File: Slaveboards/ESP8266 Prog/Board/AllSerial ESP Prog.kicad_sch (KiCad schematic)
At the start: 13 parts, among them T1 BC847, T2 BC847, X1 ALLSERIALSLAVE, X2 PinSocket_2x04_P2.54mm_Horizo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

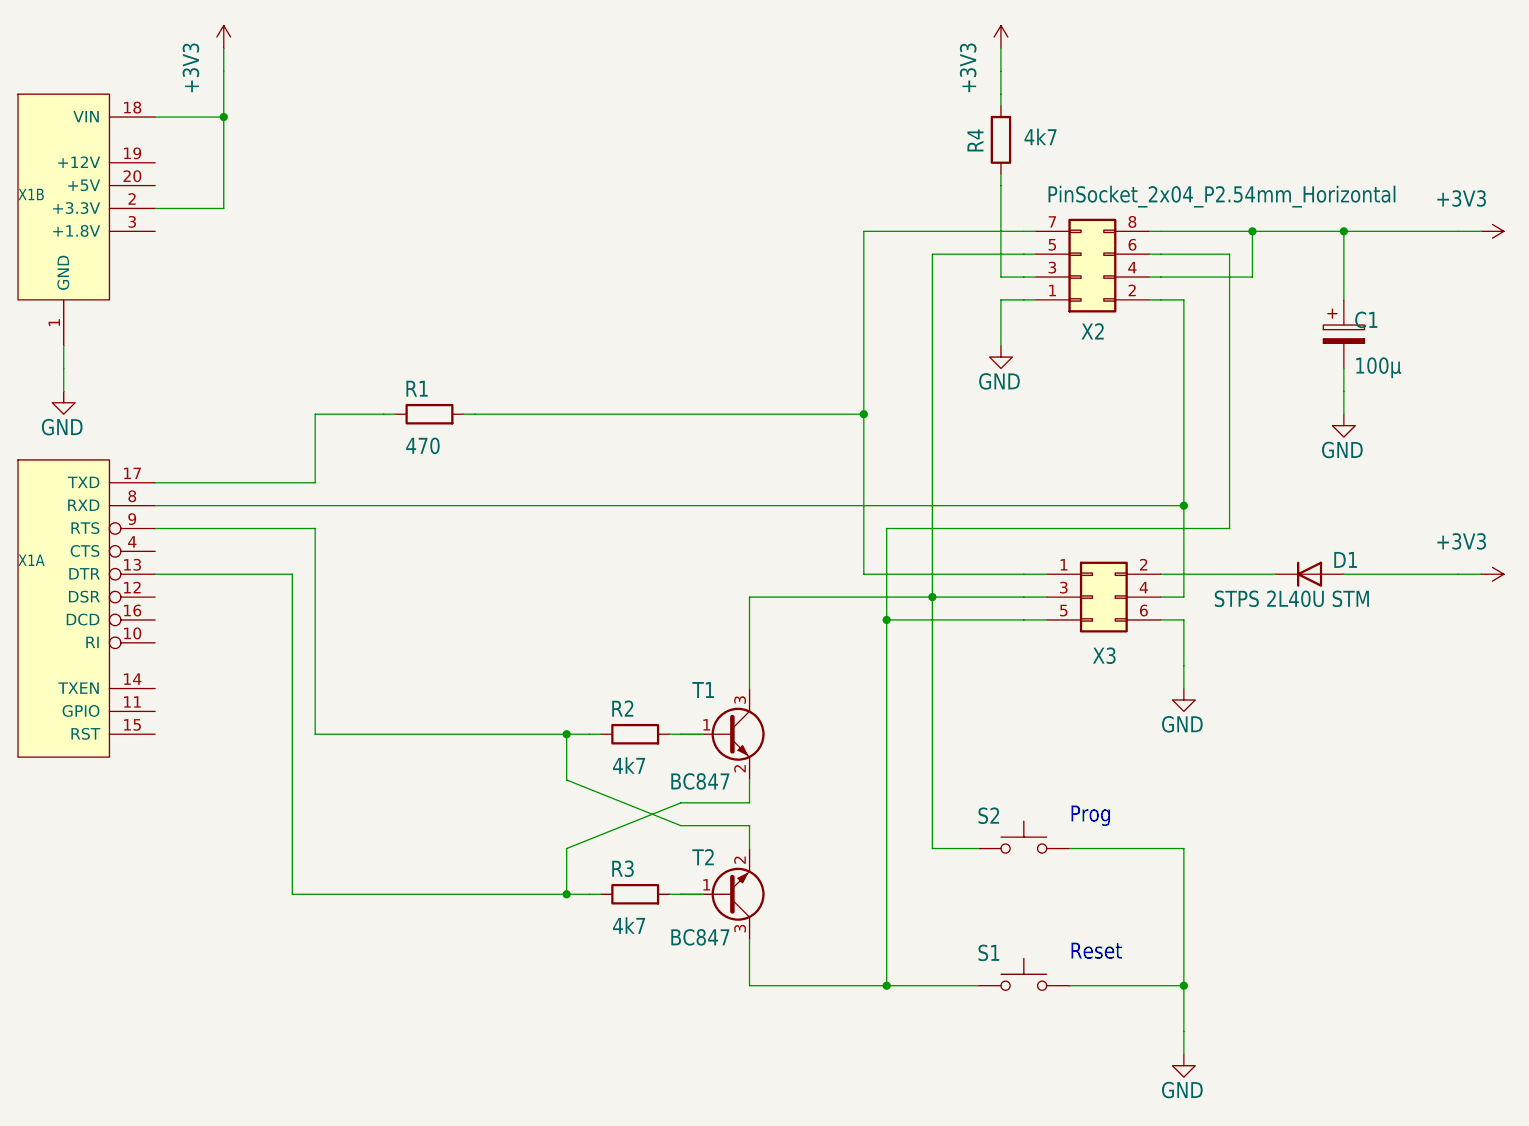
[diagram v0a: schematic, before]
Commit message: Migrate to KiCad 9
Add eBus board
Add various libraries
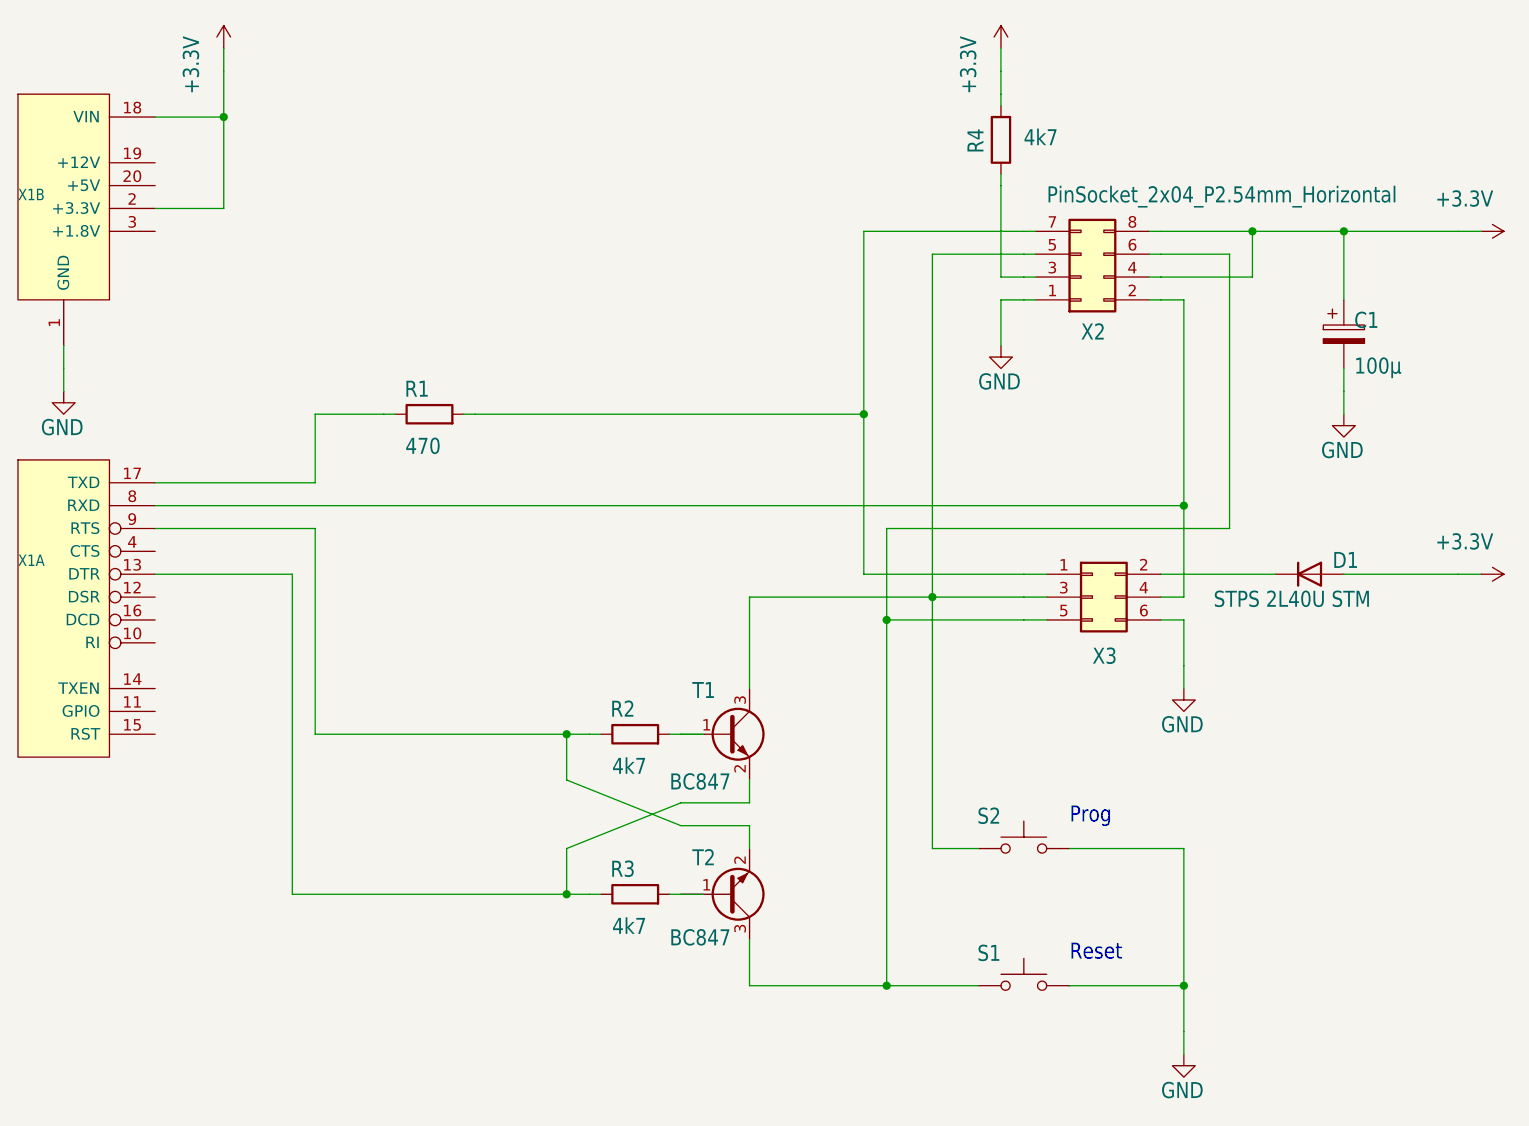
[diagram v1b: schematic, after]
